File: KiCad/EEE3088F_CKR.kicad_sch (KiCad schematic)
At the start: 0 parts

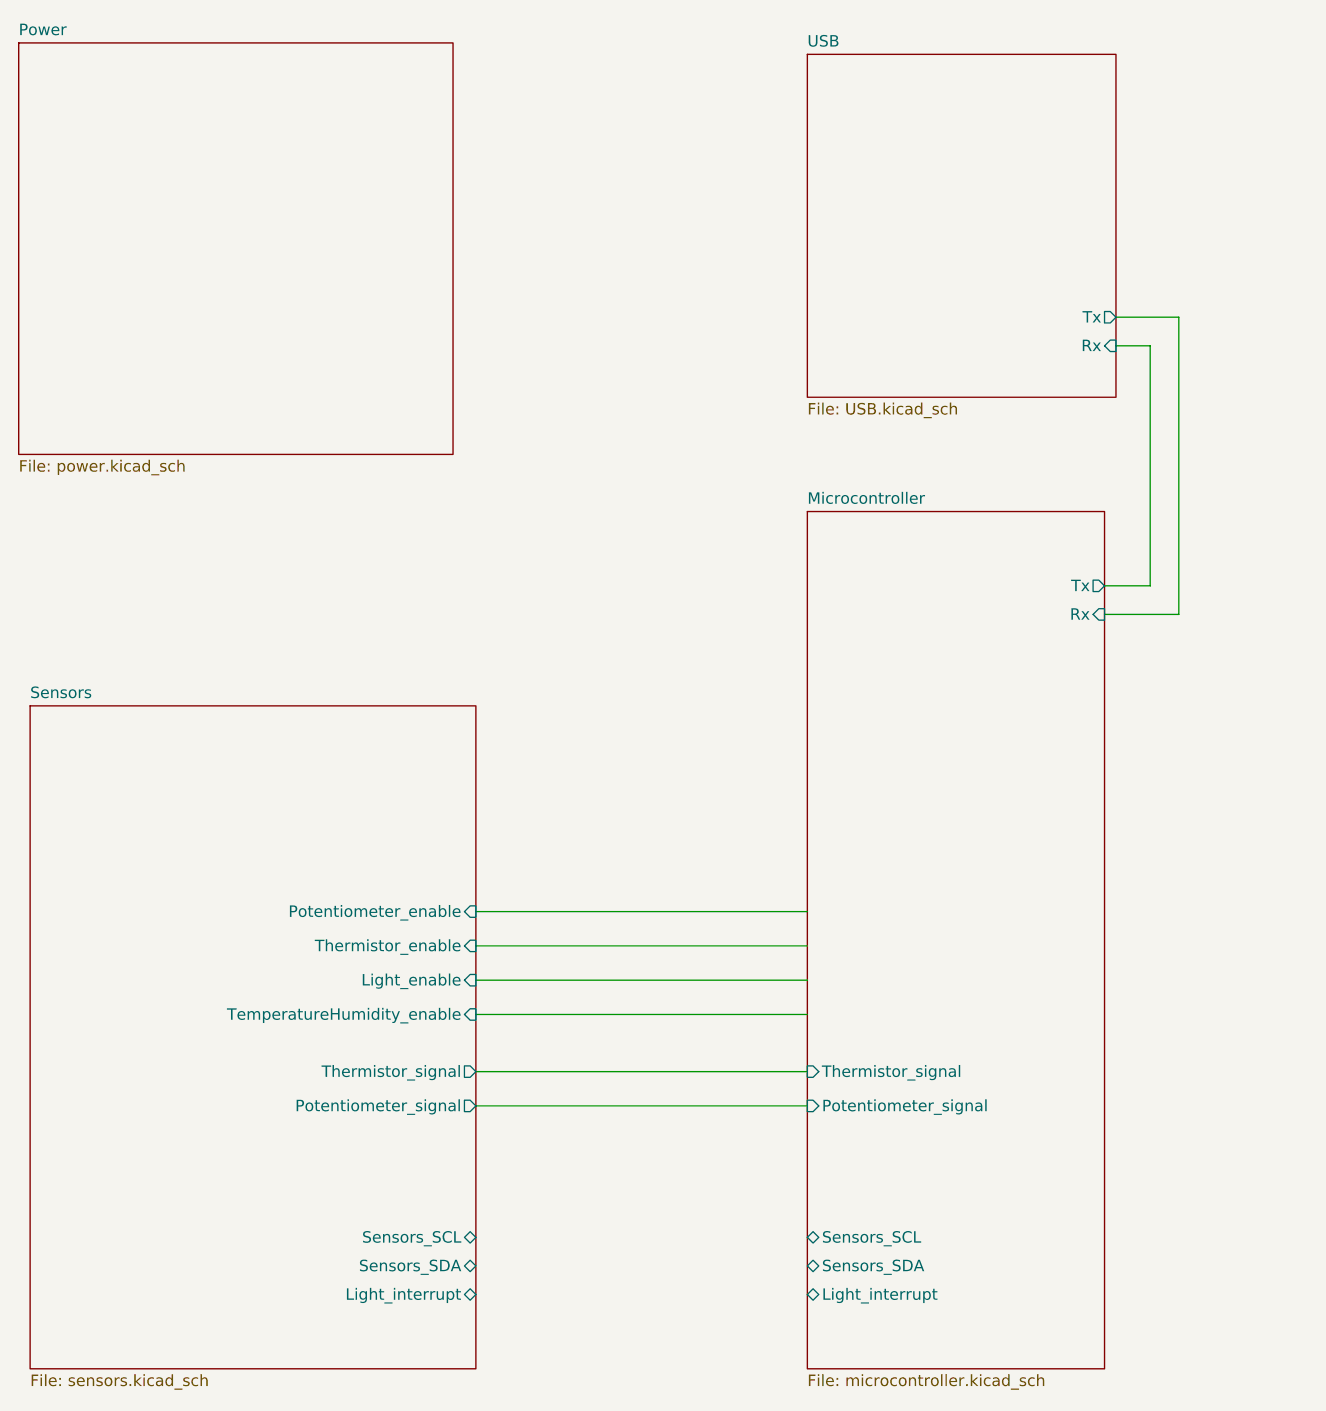
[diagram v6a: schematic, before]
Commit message: updated net labelling scheme on schematic, changed some port connections on microcontroller
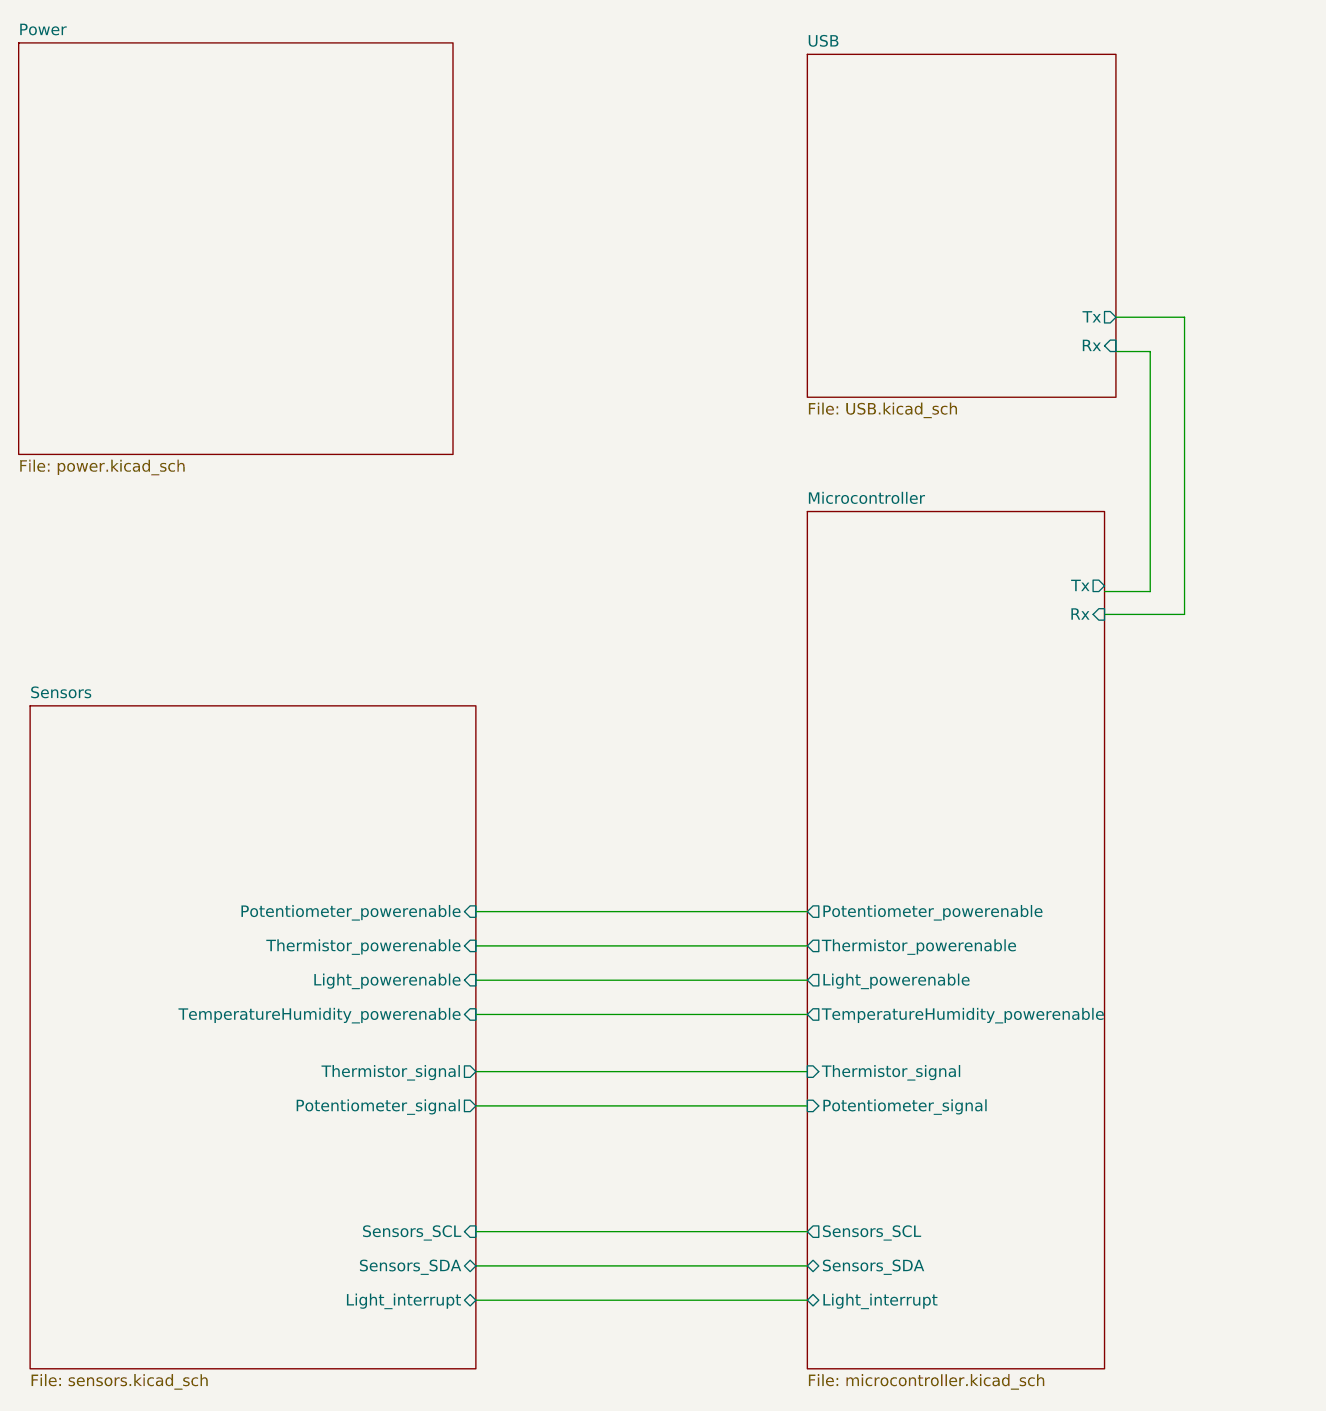
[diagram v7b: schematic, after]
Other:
- sheet Microcontroller ports: added Light_powerenable, Potentiometer_powerenable, TemperatureHumidity_powerenable, Thermistor_powerenable; removed none
- sheet Sensors ports: added Light_powerenable, Potentiometer_powerenable, TemperatureHumidity_powerenable, Thermistor_powerenable; removed Light_enable, Potentiometer_enable, TemperatureHumidity_enable, Thermistor_enable
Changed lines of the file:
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@@
     (comment 2 "This is an overview sheet showing how the sub-circuits interconnect")
   )
-  (wire (pts (xy 156.21 86.995) (xy 151.13 86.995))
+  (wire (pts (xy 156.21 87.63) (xy 151.13 87.63))
+    (stroke (width 0) (type default))
+  )
+  (wire (pts (xy 81.28 158.75) (xy 118.11 158.75))
     (stroke (width 0) (type default))
   )
@@
     (stroke (width 0) (type default))
   )
+  (wire (pts (xy 81.28 166.37) (xy 118.11 166.37))
+    (stroke (width 0) (type default))
+  )
   (wire (pts (xy 81.28 134.62) (xy 118.11 134.62))
     (stroke (width 0) (type default))
   )
-  (wire (pts (xy 159.385 90.17) (xy 159.385 57.15))
+  (wire (pts (xy 160.02 90.17) (xy 160.02 57.15))
     (stroke (width 0) (type default))
   )
@@
     (stroke (width 0) (type default))
   )
-  (wire (pts (xy 156.21 60.325) (xy 156.21 86.995))
+  (wire (pts (xy 156.21 60.96) (xy 156.21 87.63))
     (stroke (width 0) (type default))
   )
@@
     (stroke (width 0) (type default))
   )
-  (wire (pts (xy 152.4 60.325) (xy 156.21 60.325))
+  (wire (pts (xy 152.4 60.96) (xy 156.21 60.96))
     (stroke (width 0) (type default))
   )
@@
     (stroke (width 0) (type default))
   )
-  (wire (pts (xy 159.385 57.15) (xy 152.4 57.15))
+  (wire (pts (xy 160.02 57.15) (xy 152.4 57.15))
     (stroke (width 0) (type default))
   )
-  (wire (pts (xy 151.13 90.17) (xy 159.385 90.17))
+  (wire (pts (xy 81.28 162.56) (xy 118.11 162.56))
+    (stroke (width 0) (type default))
+  )
+  (wire (pts (xy 151.13 90.17) (xy 160.02 90.17))
     (stroke (width 0) (type default))
   )
@@
       (effects (font (size 1.27 1.27)) (justify left top))
     )
-    (pin "Sensors_SCL" bidirectional (at 118.11 159.385 180)
+    (pin "Sensors_SCL" output (at 118.11 158.75 180)
       (effects (font (size 1.27 1.27)) (justify left))
     )
@@
       (effects (font (size 1.27 1.27)) (justify left))
     )
-    (pin "Light_interrupt" bidirectional (at 118.11 165.735 180)
+    (pin "Light_interrupt" bidirectional (at 118.11 166.37 180)
       (effects (font (size 1.27 1.27)) (justify left))
     )
@@
     )
     (pin "Potentiometer_signal" input (at 118.11 144.78 180)
+      (effects (font (size 1.27 1.27)) (justify left))
+    )
+    (pin "Light_powerenable" output (at 118.11 130.81 180)
+      (effects (font (size 1.27 1.27)) (justify left))
+    )
+    (pin "Thermistor_powerenable" output (at 118.11 127 180)
+      (effects (font (size 1.27 1.27)) (justify left))
+    )
+    (pin "TemperatureHumidity_powerenable" output (at 118.11 134.62 180)
+      (effects (font (size 1.27 1.27)) (justify left))
+    )
+    (pin "Potentiometer_powerenable" output (at 118.11 123.19 180)
       (effects (font (size 1.27 1.27)) (justify left))
     )
@@
       (effects (font (size 1.27 1.27)) (justify left top))
     )
-    (pin "Light_interrupt" bidirectional (at 81.28 165.735 0)
+    (pin "Light_interrupt" bidirectional (at 81.28 166.37 0)
       (effects (font (size 1.27 1.27)) (justify right))
     )
@@
       (effects (font (size 1.27 1.27)) (justify right))
     )
-    (pin "Sensors_SCL" bidirectional (at 81.28 159.385 0)
+    (pin "Sensors_SCL" input (at 81.28 158.75 0)
       (effects (font (size 1.27 1.27)) (justify right))
     )
-    (pin "TemperatureHumidity_enable" input (at 81.28 134.62 0)
+    (pin "TemperatureHumidity_powerenable" input (at 81.28 134.62 0)
       (effects (font (size 1.27 1.27)) (justify right))
     )
-    (pin "Potentiometer_enable" input (at 81.28 123.19 0)
+    (pin "Thermistor_powerenable" input (at 81.28 127 0)
       (effects (font (size 1.27 1.27)) (justify right))
     )
-    (pin "Thermistor_enable" input (at 81.28 127 0)
+    (pin "Light_powerenable" input (at 81.28 130.81 0)
       (effects (font (size 1.27 1.27)) (justify right))
     )
-    (pin "Light_enable" input (at 81.28 130.81 0)
+    (pin "Potentiometer_powerenable" input (at 81.28 123.19 0)
       (effects (font (size 1.27 1.27)) (justify right))
     )

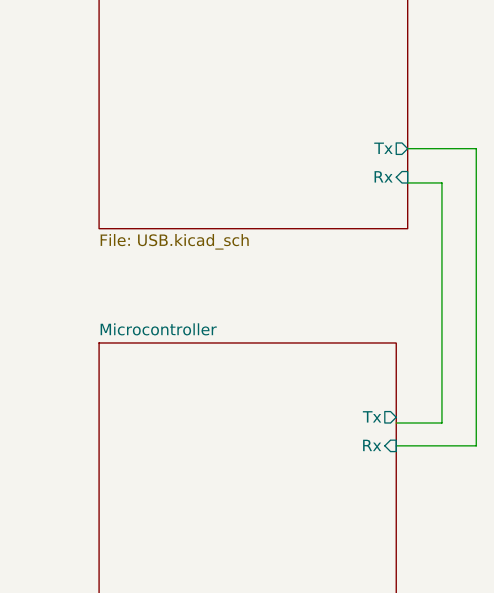
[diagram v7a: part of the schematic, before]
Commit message: ran ERCs and fixed the errors
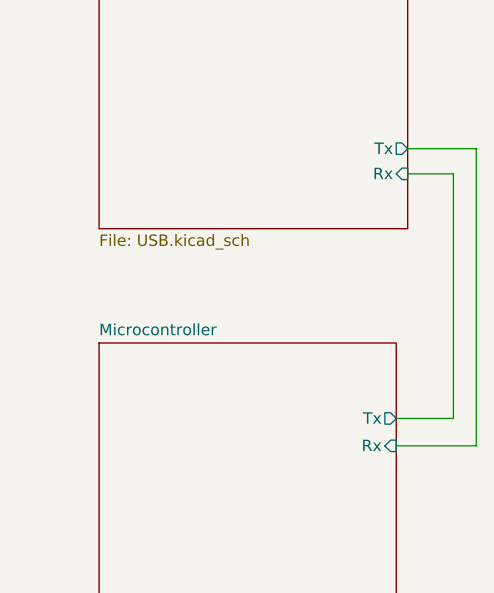
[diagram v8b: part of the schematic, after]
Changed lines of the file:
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@@
     (comment 2 "This is an overview sheet showing how the sub-circuits interconnect")
-  )
-  (wire (pts (xy 156.21 87.63) (xy 151.13 87.63))
-    (stroke (width 0) (type default))
   )
   (wire (pts (xy 81.28 158.75) (xy 118.11 158.75))
@@
     (stroke (width 0) (type default))
   )
+  (wire (pts (xy 157.48 87.122) (xy 151.13 87.122))
+    (stroke (width 0) (type default))
+  )
   (wire (pts (xy 160.02 90.17) (xy 160.02 57.15))
+    (stroke (width 0) (type default))
+  )
+  (wire (pts (xy 152.4 59.944) (xy 157.48 59.944))
     (stroke (width 0) (type default))
   )
@@
     (stroke (width 0) (type default))
   )
-  (wire (pts (xy 156.21 60.96) (xy 156.21 87.63))
-    (stroke (width 0) (type default))
-  )
   (wire (pts (xy 81.28 123.19) (xy 118.11 123.19))
-    (stroke (width 0) (type default))
-  )
-  (wire (pts (xy 152.4 60.96) (xy 156.21 60.96))
     (stroke (width 0) (type default))
   )
@@
   )
   (wire (pts (xy 160.02 57.15) (xy 152.4 57.15))
+    (stroke (width 0) (type default))
+  )
+  (wire (pts (xy 157.48 59.944) (xy 157.48 87.122))
     (stroke (width 0) (type default))
   )
@@
       (effects (font (size 1.27 1.27)) (justify right))
     )
-    (pin "Rx" input (at 152.4 60.325 0)
+    (pin "Rx" input (at 152.4 59.944 0)
       (effects (font (size 1.27 1.27)) (justify right))
     )
@@
       (effects (font (size 1.27 1.27)) (justify right))
     )
-    (pin "Tx" output (at 151.13 86.995 0)
+    (pin "Tx" output (at 151.13 87.122 0)
       (effects (font (size 1.27 1.27)) (justify right))
     )
